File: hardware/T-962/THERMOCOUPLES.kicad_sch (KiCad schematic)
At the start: 19 parts

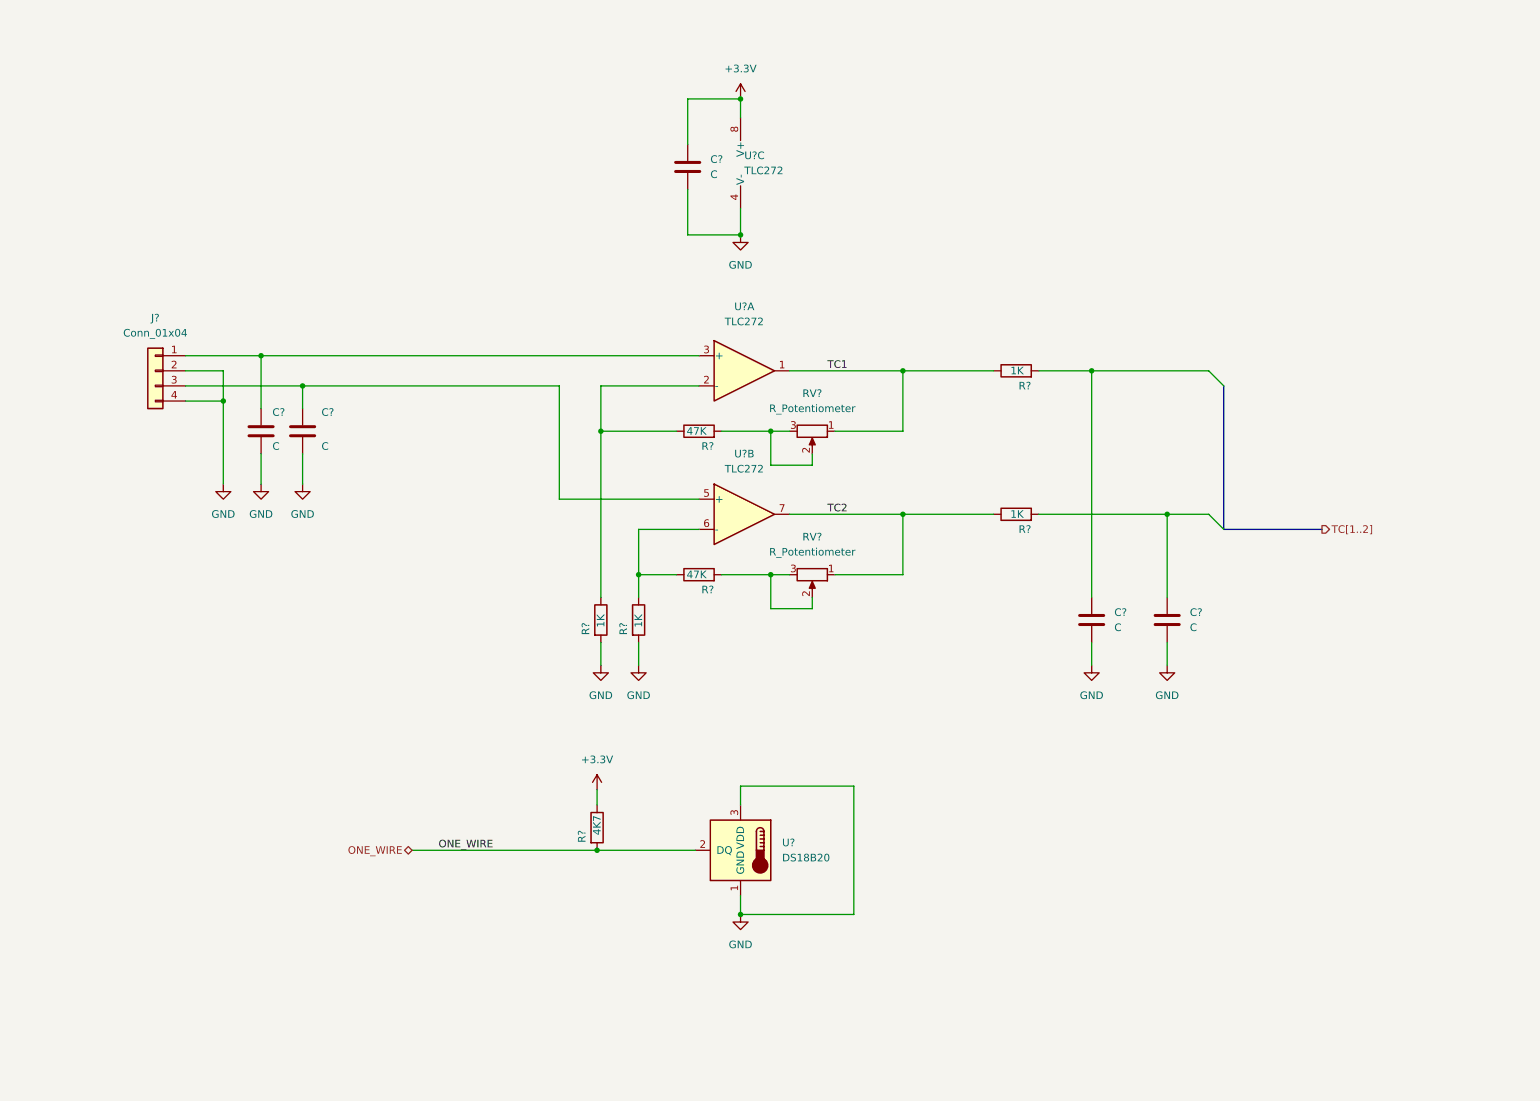
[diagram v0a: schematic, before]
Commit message: add max31850 thermocouple interfaces
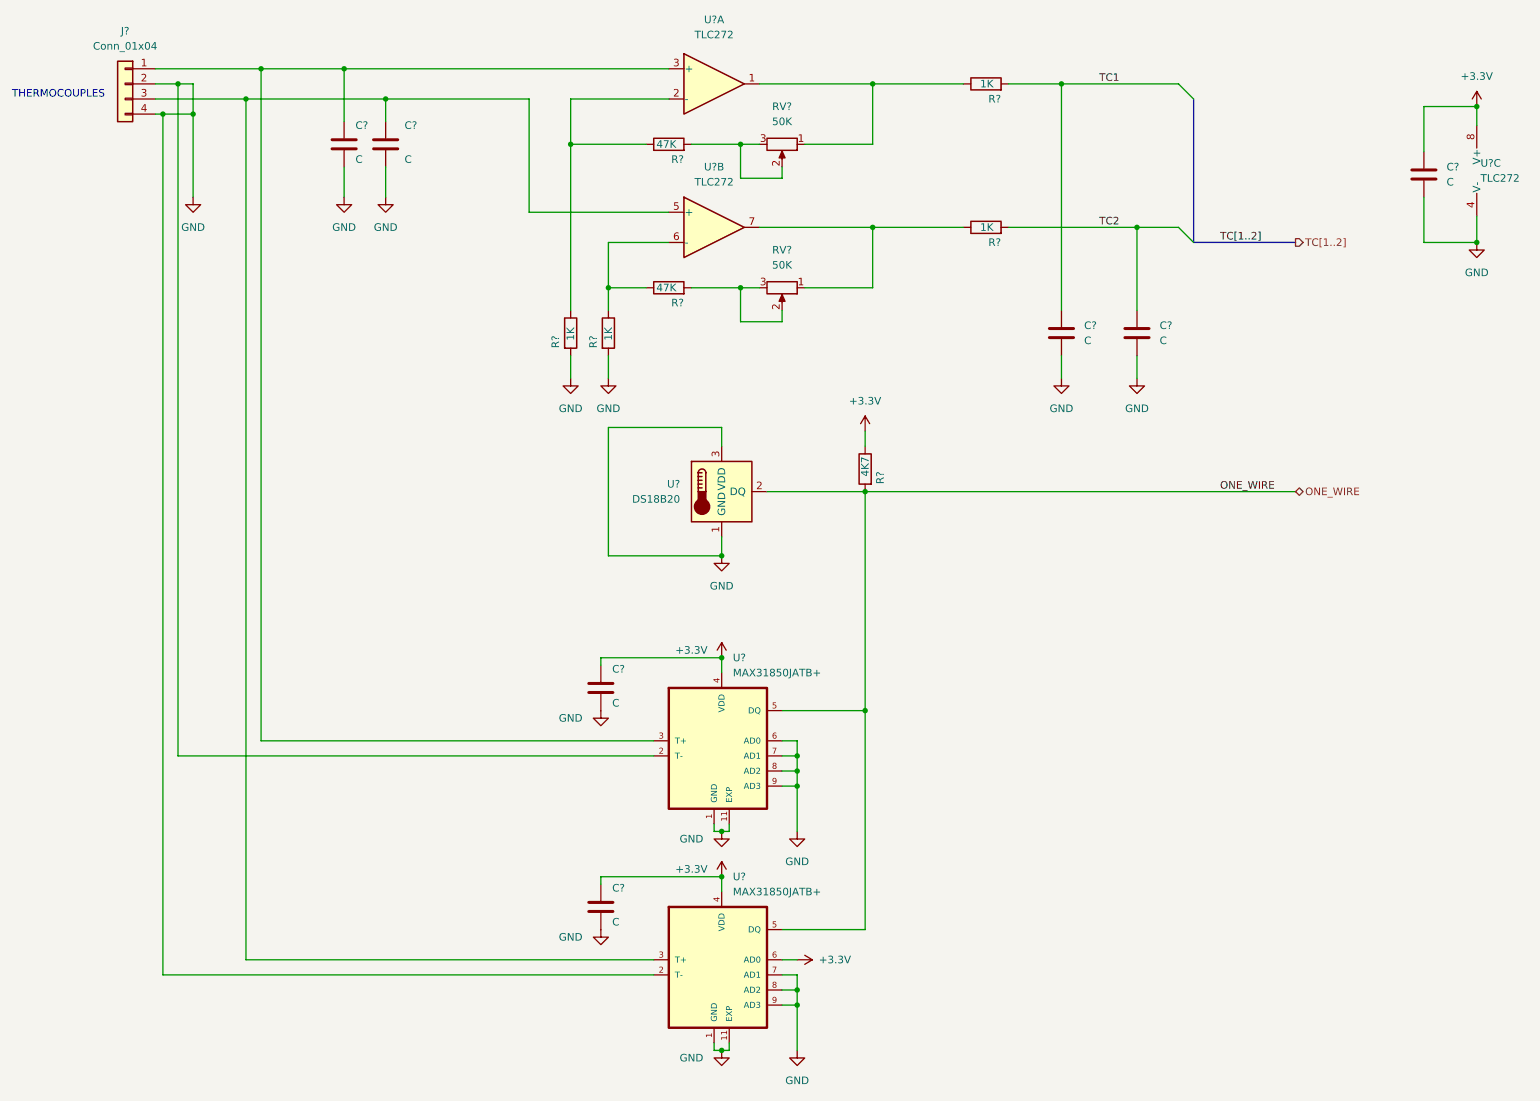
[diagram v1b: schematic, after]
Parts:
- added C? (x2): C, symbol Device:C
- added U? (x2): MAX31850JATB+, SON50P300X400X80-11N, symbol MAX31850JATB_:MAX31850JATB+
- RV? (x2): value R_Potentiometer -> 50K
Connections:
- net +3V3: now also C?.1, C?.1, U?.4 (VDD), U?.4 (VDD), U?.6 (AD0)
- net GND: now also C?.2, C?.2, U?.1 (GND), U?.1 (GND), U?.11 (EXP), U?.11 (EXP), U?.2 (T-), U?.2 (T-), U?.6 (AD0), U?.7 (AD1), U?.7 (AD1), U?.8 (AD2), U?.8 (AD2), U?.9 (AD3), U?.9 (AD3)
- net ONE_WIRE: now also U?.5 (DQ), U?.5 (DQ)
- net TC1: now also C?.1, R?.2; no longer R?.1, RV?.1, U?.1
- net TC2: now also C?.1, R?.2; no longer R?.1, RV?.1, U?.7
- net at C?.1, J?.3 (Pin_3), U?.5 (+): now also U?.3 (T+)
- net at C?.1, J?.1 (Pin_1), U?.3 (+): now also U?.3 (T+)
- new net: R?.1, RV?.1, U?.7
- new net: R?.1, RV?.1, U?.1
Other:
- note added: "THERMOCOUPLES"
- moved on the sheet: C?, J?, R?, RV?, U?, U?A, U?B, U?C

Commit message: fill out designators
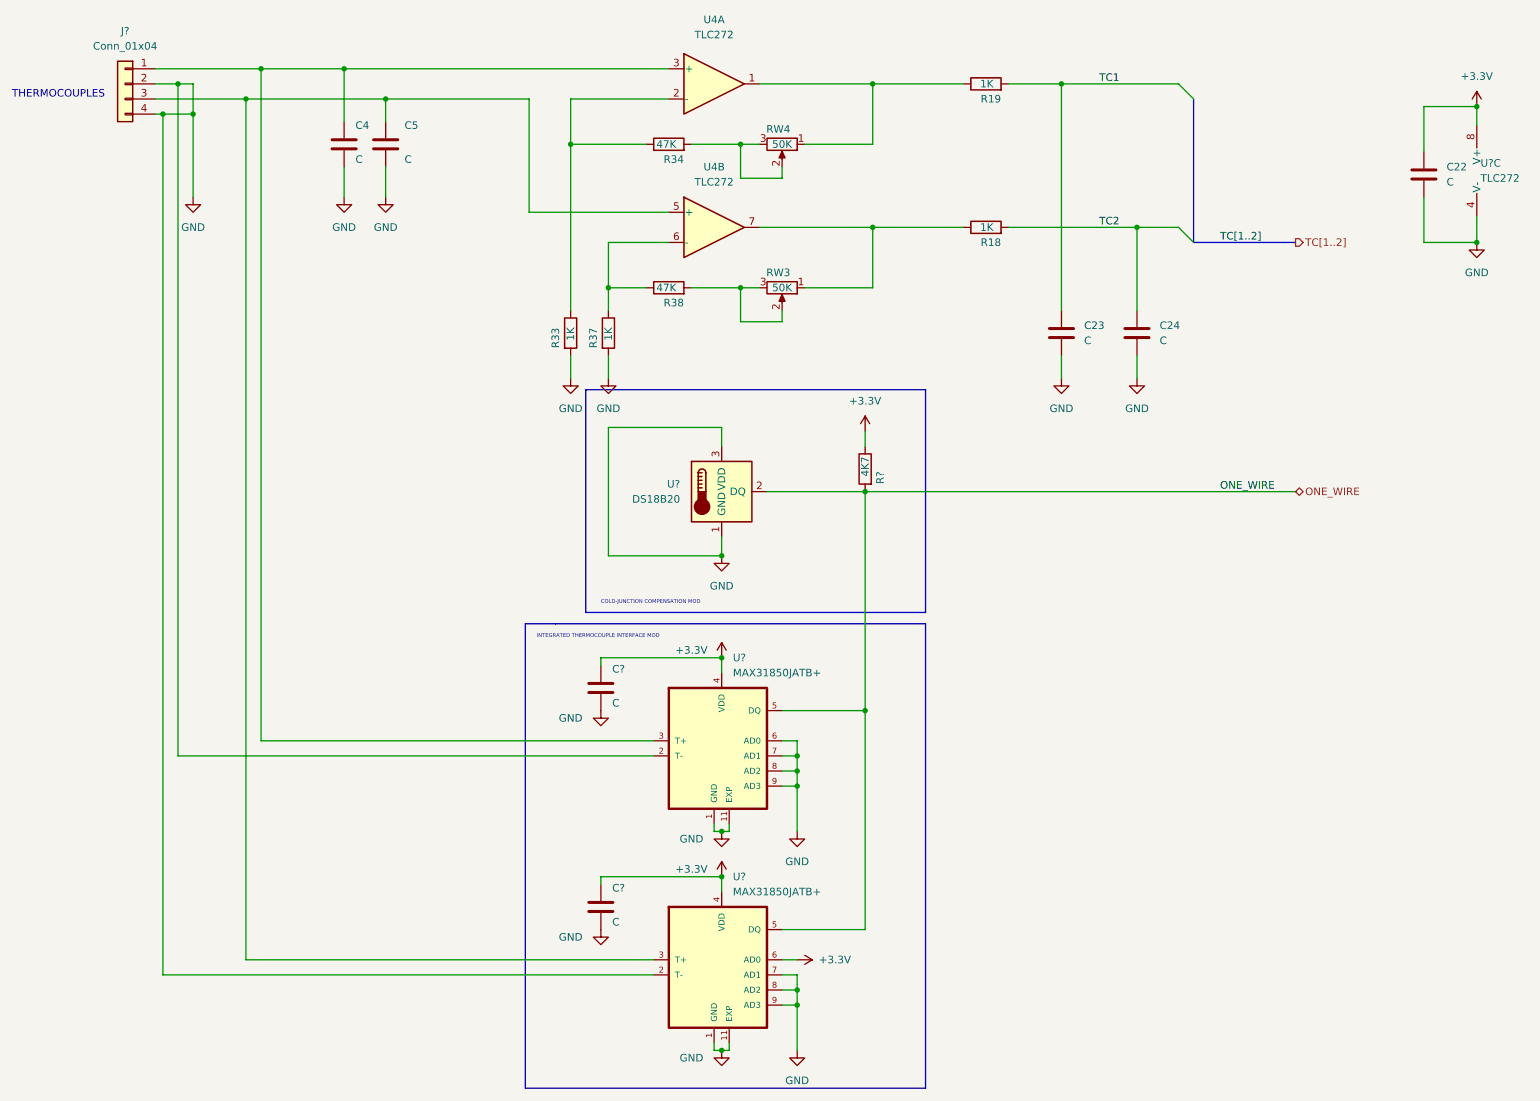
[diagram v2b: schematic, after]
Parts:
- gave numbers to parts that had none: 14
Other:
- note added: "COLD-JUNCTION COMPENSATION MOD"
- note added: "INTEGRATED THERMOCOUPLE INTERFACE MOD"
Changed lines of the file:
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@@
+    (stroke (width 0) (type default) (color 0 0 0 0))
+  )
+  (polyline (pts (xy 175.26 118.745) (xy 175.26 196.85))
     (stroke (width 0) (type default) (color 0 0 0 0))
   )
@@
     (stroke (width 0) (type default) (color 0 0 0 0))
   )
+  (polyline (pts (xy 118.11 79.375) (xy 118.11 116.84))
+    (stroke (width 0) (type default) (color 0 0 0 0))
+  )
   (wire (pts (xy 142.24 190.5) (xy 140.97 190.5))
     (stroke (width 0) (type default) (color 0 0 0 0))
@@
     (stroke (width 0) (type default) (color 0 0 0 0))
   )
+  (polyline (pts (xy 118.11 79.375) (xy 175.26 79.375))
+    (stroke (width 0) (type default) (color 0 0 0 0))
+  )
   (wire (pts (xy 144.145 43.815) (xy 144.145 38.1))
     (stroke (width 0) (type default) (color 0 0 0 0))
@@
     (stroke (width 0) (type default) (color 0 0 0 0))
   )
+  (polyline (pts (xy 175.26 196.85) (xy 107.95 196.85))
+    (stroke (width 0) (type default) (color 0 0 0 0))
+  )
   (wire (pts (xy 151.13 66.04) (xy 151.13 67.945))
     (stroke (width 0) (type default) (color 0 0 0 0))
@@
     (stroke (width 0) (type default) (color 0 0 0 0))
   )
+  (polyline (pts (xy 107.95 196.85) (xy 107.95 118.745))
+    (stroke (width 0) (type default) (color 0 0 0 0))
+  )
   (wire (pts (xy 120.65 125.73) (xy 120.65 124.46))
     (stroke (width 0) (type default) (color 0 0 0 0))
@@
     (stroke (width 0) (type default) (color 0 0 0 0))
   )
+  (polyline (pts (xy 175.26 116.84) (xy 118.11 116.84))
+    (stroke (width 0) (type default) (color 0 0 0 0))
+  )
   (wire (pts (xy 151.13 143.51) (xy 153.67 143.51))
     (stroke (width 0) (type default) (color 0 0 0 0))
@@
     (stroke (width 0) (type default) (color 0 0 0 0))
   )
+  (polyline (pts (xy 107.95 118.745) (xy 113.03 118.745))
+    (stroke (width 0) (type default) (color 0 0 0 0))
+  )
   (wire (pts (xy 45.72 33.02) (xy 46.99 33.02))
     (stroke (width 0) (type default) (color 0 0 0 0))
@@
     (stroke (width 0) (type default) (color 0 0 0 0))
   )
+  (polyline (pts (xy 175.26 79.375) (xy 175.26 116.84))
+    (stroke (width 0) (type default) (color 0 0 0 0))
+  )
+  (polyline (pts (xy 113.03 118.745) (xy 175.26 118.745))
+    (stroke (width 0) (type default) (color 0 0 0 0))
+  )
   (wire (pts (xy 115.57 38.1) (xy 128.27 38.1))
     (stroke (width 0) (type default) (color 0 0 0 0))
@@
   (wire (pts (xy 166.37 52.07) (xy 181.61 52.07))
     (stroke (width 0) (type default) (color 0 0 0 0))
+  )
+  (text "INTEGRATED THERMOCOUPLE INTERFACE MOD" (at 109.855 121.285 0)
+    (effects (font (size 0.635 0.635)) (justify left bottom))
   )
   (text "THERMOCOUPLES" (at 21.59 30.48 0)
     (effects (font (size 1.27 1.27)) (justify left bottom))
   )
+  (text "COLD-JUNCTION COMPENSATION MOD" (at 120.65 115.57 0)
+    (effects (font (size 0.635 0.635)) (justify left bottom))
+  )
   (label "ONE_WIRE" (at 224.79 96.52 0)
     (effects (font (size 1.27 1.27)) (justify left bottom))
@@
   (symbol (lib_id "Device:C") (at 84.455 38.1 0) (unit 1)
     (in_bom yes) (on_board yes)
-    (property "Reference" "C?" (id 0) (at 87.63 34.925 0)
+    (property "Reference" "C5" (id 0) (at 87.63 34.925 0)
       (effects (font (size 1.27 1.27)) (justify left))
     )
@@
   (symbol (lib_id "Amplifier_Operational:TLC272") (at 139.7 52.07 0) (unit 2)
     (in_bom yes) (on_board yes) (fields_autoplaced)
-    (property "Reference" "U?" (id 0) (at 139.7 41.91 0))
+    (property "Reference" "U4" (id 0) (at 139.7 41.91 0))
     (property "Value" "TLC272" (id 1) (at 139.7 44.45 0))
     (property "Footprint" "" (id 2) (at 139.7 52.07 0)
@@
   (symbol (lib_id "Device:R") (at 132.08 62.23 90) (unit 1)
     (in_bom yes) (on_board yes)
-    (property "Reference" "R?" (id 0) (at 134.62 64.77 90)
+    (property "Reference" "R38" (id 0) (at 134.62 64.77 90)
       (effects (font (size 1.27 1.27)) (justify left))
     )
@@
   (symbol (lib_id "Device:C") (at 77.47 38.1 0) (unit 1)
     (in_bom yes) (on_board yes)
-    (property "Reference" "C?" (id 0) (at 79.375 34.925 0)
+    (property "Reference" "C4" (id 0) (at 79.375 34.925 0)
       (effects (font (size 1.27 1.27)) (justify left))
     )
@@
   (symbol (lib_id "Device:R") (at 115.57 69.85 0) (unit 1)
     (in_bom yes) (on_board yes)
-    (property "Reference" "R?" (id 0) (at 113.03 72.39 90)
+    (property "Reference" "R33" (id 0) (at 113.03 72.39 90)
       (effects (font (size 1.27 1.27)) (justify left))
     )
@@
   (symbol (lib_id "Device:C") (at 259.08 43.18 0) (unit 1)
     (in_bom yes) (on_board yes) (fields_autoplaced)
-    (property "Reference" "C?" (id 0) (at 262.89 41.9099 0)
+    (property "Reference" "C22" (id 0) (at 262.89 41.9099 0)
       (effects (font (size 1.27 1.27)) (justify left))
     )
@@
   (symbol (lib_id "Device:R") (at 121.92 69.85 0) (unit 1)
     (in_bom yes) (on_board yes)
-    (property "Reference" "R?" (id 0) (at 119.38 72.39 90)
+    (property "Reference" "R37" (id 0) (at 119.38 72.39 90)
       (effects (font (size 1.27 1.27)) (justify left))
     )
@@
   (symbol (lib_id "Device:C") (at 210.82 69.85 0) (unit 1)
     (in_bom yes) (on_board yes) (fields_autoplaced)
-    (property "Reference" "C?" (id 0) (at 214.63 68.5799 0)
+    (property "Reference" "C24" (id 0) (at 214.63 68.5799 0)
       (effects (font (size 1.27 1.27)) (justify left))
     )
@@
   (symbol (lib_id "Device:R") (at 185.42 52.07 90) (unit 1)
     (in_bom yes) (on_board yes)
-    (property "Reference" "R?" (id 0) (at 187.96 54.61 90)
+    (property "Reference" "R18" (id 0) (at 187.96 54.61 90)
       (effects (font (size 1.27 1.27)) (justify left))
     )
@@
   (symbol (lib_id "Device:R") (at 132.08 38.1 90) (unit 1)
     (in_bom yes) (on_board yes)
-    (property "Reference" "R?" (id 0) (at 134.62 40.64 90)
+    (property "Reference" "R34" (id 0) (at 134.62 40.64 90)
       (effects (font (size 1.27 1.27)) (justify left))
     )
@@
   (symbol (lib_id "Amplifier_Operational:TLC272") (at 139.7 27.94 0) (unit 1)
     (in_bom yes) (on_board yes) (fields_autoplaced)
-    (property "Reference" "U?" (id 0) (at 139.7 17.145 0))
+    (property "Reference" "U4" (id 0) (at 139.7 17.145 0))
     (property "Value" "TLC272" (id 1) (at 139.7 19.685 0))
     (property "Footprint" "" (id 2) (at 139.7 27.94 0)
@@
   (symbol (lib_id "Device:C") (at 198.12 69.85 0) (unit 1)
     (in_bom yes) (on_board yes) (fields_autoplaced)
-    (property "Reference" "C?" (id 0) (at 201.93 68.5799 0)
+    (property "Reference" "C23" (id 0) (at 201.93 68.5799 0)
       (effects (font (size 1.27 1.27)) (justify left))
     )
@@
   )
   (symbol (lib_id "Device:R_Potentiometer") (at 151.13 62.23 270) (unit 1)
-    (in_bom yes) (on_board yes) (fields_autoplaced)
-    (property "Reference" "RV?" (id 0) (at 151.13 55.88 90))
-    (property "Value" "50K" (id 1) (at 151.13 58.42 90))
+    (in_bom yes) (on_board yes)
+    (property "Reference" "RW3" (id 0) (at 150.495 59.69 90))
+    (property "Value" "50K" (id 1) (at 151.13 62.23 90))
     (property "Footprint" "" (id 2) (at 151.13 62.23 0)
       (effects (font (size 1.27 1.27)) hide)
@@
   (symbol (lib_id "Device:R") (at 185.42 27.94 90) (unit 1)
     (in_bom yes) (on_board yes)
-    (property "Reference" "R?" (id 0) (at 187.96 30.48 90)
+    (property "Reference" "R19" (id 0) (at 187.96 30.48 90)
       (effects (font (size 1.27 1.27)) (justify left))
     )
@@
   )
   (symbol (lib_id "Device:R_Potentiometer") (at 151.13 38.1 270) (unit 1)
-    (in_bom yes) (on_board yes) (fields_autoplaced)
-    (property "Reference" "RV?" (id 0) (at 151.13 31.75 90))
-    (property "Value" "50K" (id 1) (at 151.13 34.29 90))
+    (in_bom yes) (on_board yes)
+    (property "Reference" "RW4" (id 0) (at 150.495 35.56 90))
+    (property "Value" "50K" (id 1) (at 151.13 38.1 90))
     (property "Footprint" "" (id 2) (at 151.13 38.1 0)
       (effects (font (size 1.27 1.27)) hide)
